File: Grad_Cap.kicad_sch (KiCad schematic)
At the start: 86 parts, among them U1 ItsyBitsy 32u4 5V

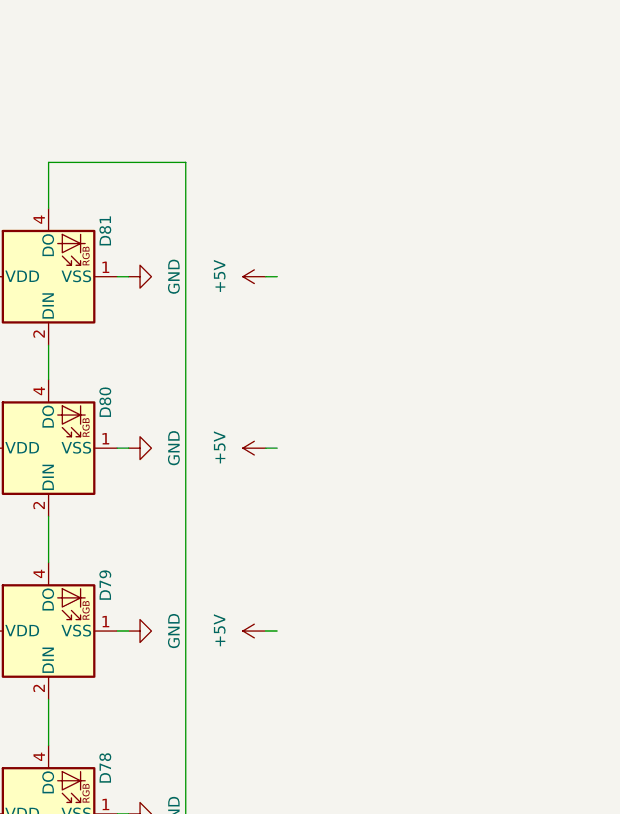
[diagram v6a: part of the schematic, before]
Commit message: cap + refs gone
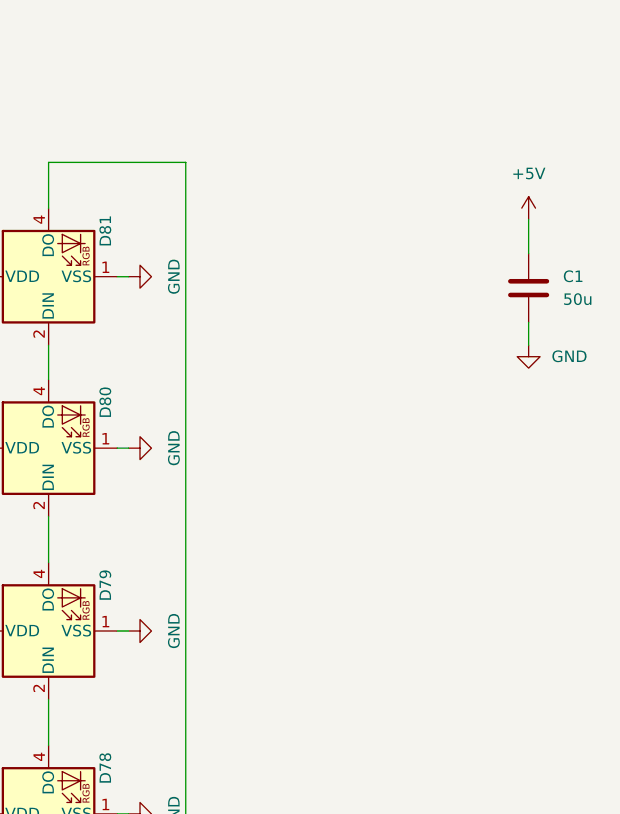
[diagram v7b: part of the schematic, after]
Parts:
- added C1: 50u, Capacitor_SMD:C_1206_3216Metric_Pad1.33x1.80mm_HandSolder, symbol Device:C
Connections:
- net +5V: now also C1.1
- net GND: now also C1.2
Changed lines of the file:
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@@
     (stroke (width 0) (type default) (color 0 0 0 0))
   )
-  (wire (pts (xy 332.74 93.98) (xy 334.01 93.98))
-    (stroke (width 0) (type default) (color 0 0 0 0))
-  )
   (wire (pts (xy 185.42 267.97) (xy 185.42 269.24))
     (stroke (width 0) (type default) (color 0 0 0 0))
@@
     (stroke (width 0) (type default) (color 0 0 0 0))
   )
-  (wire (pts (xy 332.74 54.61) (xy 334.01 54.61))
-    (stroke (width 0) (type default) (color 0 0 0 0))
-  )
   (wire (pts (xy 204.47 119.38) (xy 204.47 120.65))
     (stroke (width 0) (type default) (color 0 0 0 0))
@@
     (stroke (width 0) (type default) (color 0 0 0 0))
   )
+  (wire (pts (xy 361.95 48.26) (xy 361.95 52.07))
+    (stroke (width 0) (type default) (color 0 0 0 0))
+  )
   (wire (pts (xy 52.07 44.45) (xy 58.42 44.45))
     (stroke (width 0) (type default) (color 0 0 0 0))
@@
     (stroke (width 0) (type default) (color 0 0 0 0))
   )
-  (wire (pts (xy 332.74 73.66) (xy 334.01 73.66))
-    (stroke (width 0) (type default) (color 0 0 0 0))
-  )
   (wire (pts (xy 332.74 212.09) (xy 334.01 212.09))
     (stroke (width 0) (type default) (color 0 0 0 0))
@@
     (stroke (width 0) (type default) (color 0 0 0 0))
   )
+  (wire (pts (xy 361.95 59.69) (xy 361.95 62.23))
+    (stroke (width 0) (type default) (color 0 0 0 0))
+  )
   (wire (pts (xy 88.9 49.53) (xy 58.42 49.53))
     (stroke (width 0) (type default) (color 0 0 0 0))
@@
     (pin "1")
   )
+  (symbol (lib_id "power:GND") (at 361.95 62.23 0) (unit 1)
+    (in_bom yes) (on_board yes) (fields_autoplaced)
+    (property "Reference" "#PWR0251" (id 0) (at 361.95 68.58 0)
+      (effects (font (size 1.27 1.27)) hide)
+    )
+    (property "Value" "GND" (id 1) (at 364.49 63.4999 0)
+      (effects (font (size 1.27 1.27)) (justify left))
+    )
+    (property "Footprint" "" (id 2) (at 361.95 62.23 0)
+      (effects (font (size 1.27 1.27)) hide)
+    )
+    (property "Datasheet" "" (id 3) (at 361.95 62.23 0)
+      (effects (font (size 1.27 1.27)) hide)
+    )
+    (pin "1")
+  )
   (symbol (lib_id "power:GND") (at 204.47 137.16 0) (unit 1)
     (in_bom yes) (on_board yes) (fields_autoplaced)
@@
     (pin "4")
   )
-  (symbol (lib_id "power:+5V") (at 332.74 54.61 90) (unit 1)
+  (symbol (lib_id "power:+5V") (at 361.95 48.26 0) (unit 1)
     (in_bom yes) (on_board yes) (fields_autoplaced)
-    (property "Reference" "#PWR0250" (id 0) (at 336.55 54.61 0)
+    (property "Reference" "#PWR0250" (id 0) (at 361.95 52.07 0)
       (effects (font (size 1.27 1.27)) hide)
     )
-    (property "Value" "+5V" (id 1) (at 327.66 54.61 0))
-    (property "Footprint" "" (id 2) (at 332.74 54.61 0)
+    (property "Value" "+5V" (id 1) (at 361.95 43.18 0))
+    (property "Footprint" "" (id 2) (at 361.95 48.26 0)
       (effects (font (size 1.27 1.27)) hide)
     )
-    (property "Datasheet" "" (id 3) (at 332.74 54.61 0)
+    (property "Datasheet" "" (id 3) (at 361.95 48.26 0)
       (effects (font (size 1.27 1.27)) hide)
     )
@@
     (pin "4")
   )
+  (symbol (lib_id "Device:C") (at 361.95 55.88 0) (unit 1)
+    (in_bom yes) (on_board yes) (fields_autoplaced)
+    (property "Reference" "C1" (id 0) (at 365.76 54.6099 0)
+      (effects (font (size 1.27 1.27)) (justify left))
+    )
+    (property "Value" "50u" (id 1) (at 365.76 57.1499 0)
+      (effects (font (size 1.27 1.27)) (justify left))
+    )
+    (property "Footprint" "Capacitor_SMD:C_1206_3216Metric_Pad1.33x1.80mm_HandSolder" (id 2) (at 362.9152 59.69 0)
+      (effects (font (size 1.27 1.27)) hide)
+    )
+    (property "Datasheet" "~" (id 3) (at 361.95 55.88 0)
+      (effects (font (size 1.27 1.27)) hide)
+    )
+    (pin "1")
+    (pin "2")
+  )
   (symbol (lib_id "LED:Inolux_IN-PI554FCH") (at 185.42 161.29 0) (unit 1)
     (in_bom yes) (on_board yes)
@@
     (pin "1")
   )
-  (symbol (lib_id "power:+5V") (at 332.74 73.66 90) (unit 1)
-    (in_bom yes) (on_board yes) (fields_autoplaced)
-    (property "Reference" "#PWR0252" (id 0) (at 336.55 73.66 0)
-      (effects (font (size 1.27 1.27)) hide)
-    )
-    (property "Value" "+5V" (id 1) (at 327.66 73.66 0))
-    (property "Footprint" "" (id 2) (at 332.74 73.66 0)
-      (effects (font (size 1.27 1.27)) hide)
-    )
-    (property "Datasheet" "" (id 3) (at 332.74 73.66 0)
-      (effects (font (size 1.27 1.27)) hide)
-    )
-    (pin "1")
-  )
   (symbol (lib_id "power:GND") (at 106.68 170.18 0) (unit 1)
     (in_bom yes) (on_board yes) (fields_autoplaced)
@@
     (pin "4")
   )
-  (symbol (lib_id "power:+5V") (at 332.74 93.98 90) (unit 1)
-    (in_bom yes) (on_board yes) (fields_autoplaced)
-    (property "Reference" "#PWR0251" (id 0) (at 336.55 93.98 0)
-      (effects (font (size 1.27 1.27)) hide)
-    )
-    (property "Value" "+5V" (id 1) (at 327.66 93.98 0))
-    (property "Footprint" "" (id 2) (at 332.74 93.98 0)
-      (effects (font (size 1.27 1.27)) hide)
-    )
-    (property "Datasheet" "" (id 3) (at 332.74 93.98 0)
-      (effects (font (size 1.27 1.27)) hide)
-    )
-    (pin "1")
-  )
   (symbol (lib_id "power:+5V") (at 332.74 153.67 90) (unit 1)
     (in_bom yes) (on_board yes) (fields_autoplaced)
@@
       (reference "#PWR0250") (unit 1) (value "+5V") (footprint "")
     )
-    (path "/ee4570be-4d0c-4443-b7f3-6f023788781f"
-      (reference "#PWR0251") (unit 1) (value "+5V") (footprint "")
-    )
-    (path "/ce5632bc-e00c-45f4-b14e-825b7ef292f1"
-      (reference "#PWR0252") (unit 1) (value "+5V") (footprint "")
+    (path "/24c4946d-ae57-413b-abd0-9584a6aab33d"
+      (reference "#PWR0251") (unit 1) (value "GND") (footprint "")
     )
     (path "/852985ea-369e-4d31-bb9e-c95be0364da6"
@@
       (reference "#PWR0277") (unit 1) (value "GND") (footprint "")
     )
+    (path "/91976d85-679e-4d4e-8538-c0f5d7e5a2b6"
+      (reference "C1") (unit 1) (value "50u") (footprint "Capacitor_SMD:C_1206_3216Metric_Pad1.33x1.80mm_HandSolder")
+    )
     (path "/da11b958-4a02-4791-8044-007862b622ee"

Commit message: Pads Added
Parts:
- added TP1, TP2: TestPoint, TestPoint:TestPoint_Pad_4.0x4.0mm, symbol Connector:TestPoint
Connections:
- net +5V: now also TP1.1
- net GND: now also TP2.1
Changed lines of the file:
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@@
     (stroke (width 0) (type default) (color 0 0 0 0))
   )
+  (wire (pts (xy 341.63 90.17) (xy 341.63 92.71))
+    (stroke (width 0) (type default) (color 0 0 0 0))
+  )
   (wire (pts (xy 153.67 260.35) (xy 157.48 260.35))
     (stroke (width 0) (type default) (color 0 0 0 0))
@@
     (stroke (width 0) (type default) (color 0 0 0 0))
   )
+  (wire (pts (xy 350.52 92.71) (xy 350.52 95.25))
+    (stroke (width 0) (type default) (color 0 0 0 0))
+  )
   (wire (pts (xy 99.06 110.49) (xy 276.86 110.49))
     (stroke (width 0) (type default) (color 0 0 0 0))
@@
     (pin "1")
   )
+  (symbol (lib_id "power:+5V") (at 341.63 90.17 0) (unit 1)
+    (in_bom yes) (on_board yes) (fields_autoplaced)
+    (property "Reference" "#PWR0252" (id 0) (at 341.63 93.98 0)
+      (effects (font (size 1.27 1.27)) hide)
+    )
+    (property "Value" "+5V" (id 1) (at 341.63 85.09 0))
+    (property "Footprint" "" (id 2) (at 341.63 90.17 0)
+      (effects (font (size 1.27 1.27)) hide)
+    )
+    (property "Datasheet" "" (id 3) (at 341.63 90.17 0)
+      (effects (font (size 1.27 1.27)) hide)
+    )
+    (pin "1")
+  )
   (symbol (lib_id "power:+5V") (at 264.16 218.44 0) (unit 1)
     (in_bom yes) (on_board yes) (fields_autoplaced)
@@
     (pin "1")
   )
+  (symbol (lib_id "Connector:TestPoint") (at 341.63 92.71 180) (unit 1)
+    (in_bom yes) (on_board yes) (fields_autoplaced)
+    (property "Reference" "TP1" (id 0) (at 344.17 94.7419 0)
+      (effects (font (size 1.27 1.27)) (justify right))
+    )
+    (property "Value" "TestPoint" (id 1) (at 344.17 97.2819 0)
+      (effects (font (size 1.27 1.27)) (justify right))
+    )
+    (property "Footprint" "TestPoint:TestPoint_Pad_4.0x4.0mm" (id 2) (at 336.55 92.71 0)
+      (effects (font (size 1.27 1.27)) hide)
+    )
+    (property "Datasheet" "~" (id 3) (at 336.55 92.71 0)
+      (effects (font (size 1.27 1.27)) hide)
+    )
+    (pin "1")
+  )
   (symbol (lib_id "power:+5V") (at 185.42 20.32 0) (unit 1)
     (in_bom yes) (on_board yes) (fields_autoplaced)
@@
     (pin "4")
   )
+  (symbol (lib_name "GND_3") (lib_id "power:GND") (at 350.52 95.25 0) (unit 1)
+    (in_bom yes) (on_board yes) (fields_autoplaced)
+    (property "Reference" "#PWR0258" (id 0) (at 350.52 101.6 0)
+      (effects (font (size 1.27 1.27)) hide)
+    )
+    (property "Value" "GND" (id 1) (at 350.52 100.33 0))
+    (property "Footprint" "" (id 2) (at 350.52 95.25 0)
+      (effects (font (size 1.27 1.27)) hide)
+    )
+    (property "Datasheet" "" (id 3) (at 350.52 95.25 0)
+      (effects (font (size 1.27 1.27)) hide)
+    )
+    (pin "1")
+  )
   (symbol (lib_id "power:+5V") (at 185.42 86.36 0) (unit 1)
     (in_bom yes) (on_board yes) (fields_autoplaced)
@@
     (pin "1")
   )
+  (symbol (lib_id "Connector:TestPoint") (at 350.52 92.71 0) (unit 1)
+    (in_bom yes) (on_board yes) (fields_autoplaced)
+    (property "Reference" "TP2" (id 0) (at 353.06 88.1379 0)
+      (effects (font (size 1.27 1.27)) (justify left))
+    )
+    (property "Value" "TestPoint" (id 1) (at 353.06 90.6779 0)
+      (effects (font (size 1.27 1.27)) (justify left))
+    )
+    (property "Footprint" "TestPoint:TestPoint_Pad_4.0x4.0mm" (id 2) (at 355.6 92.71 0)
+      (effects (font (size 1.27 1.27)) hide)
+    )
+    (property "Datasheet" "" (id 3) (at 355.6 92.71 0)
+      (effects (font (size 1.27 1.27)) hide)
+    )
+    (pin "1")
+  )
   (symbol (lib_id "LED:Inolux_IN-PI554FCH") (at 106.68 194.31 0) (unit 1)
     (in_bom yes) (on_board yes)
@@
       (reference "#PWR0251") (unit 1) (value "GND") (footprint "")
     )
+    (path "/6e3dc5c3-5494-438e-85ba-85658666f454"
+      (reference "#PWR0252") (unit 1) (value "+5V") (footprint "")
+    )
     (path "/852985ea-369e-4d31-bb9e-c95be0364da6"
       (reference "#PWR0253") (unit 1) (value "GND") (footprint "")
@@
       (reference "#PWR0257") (unit 1) (value "+5V") (footprint "")
     )
+    (path "/b6d10b3f-cd5f-42de-8bae-814eda85ca94"
+      (reference "#PWR0258") (unit 1) (value "GND") (footprint "")
+    )
     (path "/f2736d4f-41f0-49d6-a9c4-4f4f883f740c"
       (reference "#PWR0259") (unit 1) (value "GND") (footprint "")
@@
       (reference "R1") (unit 1) (value "330") (footprint "Resistor_SMD:R_1206_3216Metric_Pad1.30x1.75mm_HandSolder")
     )
+    (path "/9dde1d2c-cc43-4a60-a255-4b69425034cd"
+      (reference "TP1") (unit 1) (value "TestPoint") (footprint "TestPoint:TestPoint_Pad_4.0x4.0mm")
+    )
+    (path "/e9451162-8d27-4470-a40b-6d1bbf8f550f"
+      (reference "TP2") (unit 1) (value "TestPoint") (footprint "TestPoint:TestPoint_Pad_4.0x4.0mm")
+    )
     (path "/a5c46b29-3091-45c4-b411-8345b67a7d70"
